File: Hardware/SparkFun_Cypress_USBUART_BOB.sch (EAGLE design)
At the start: 29 parts, among them J1 MICROB, J3 FTDI_BASICPTH, U1 CY7C65213, U2 MIC5219 3.3V

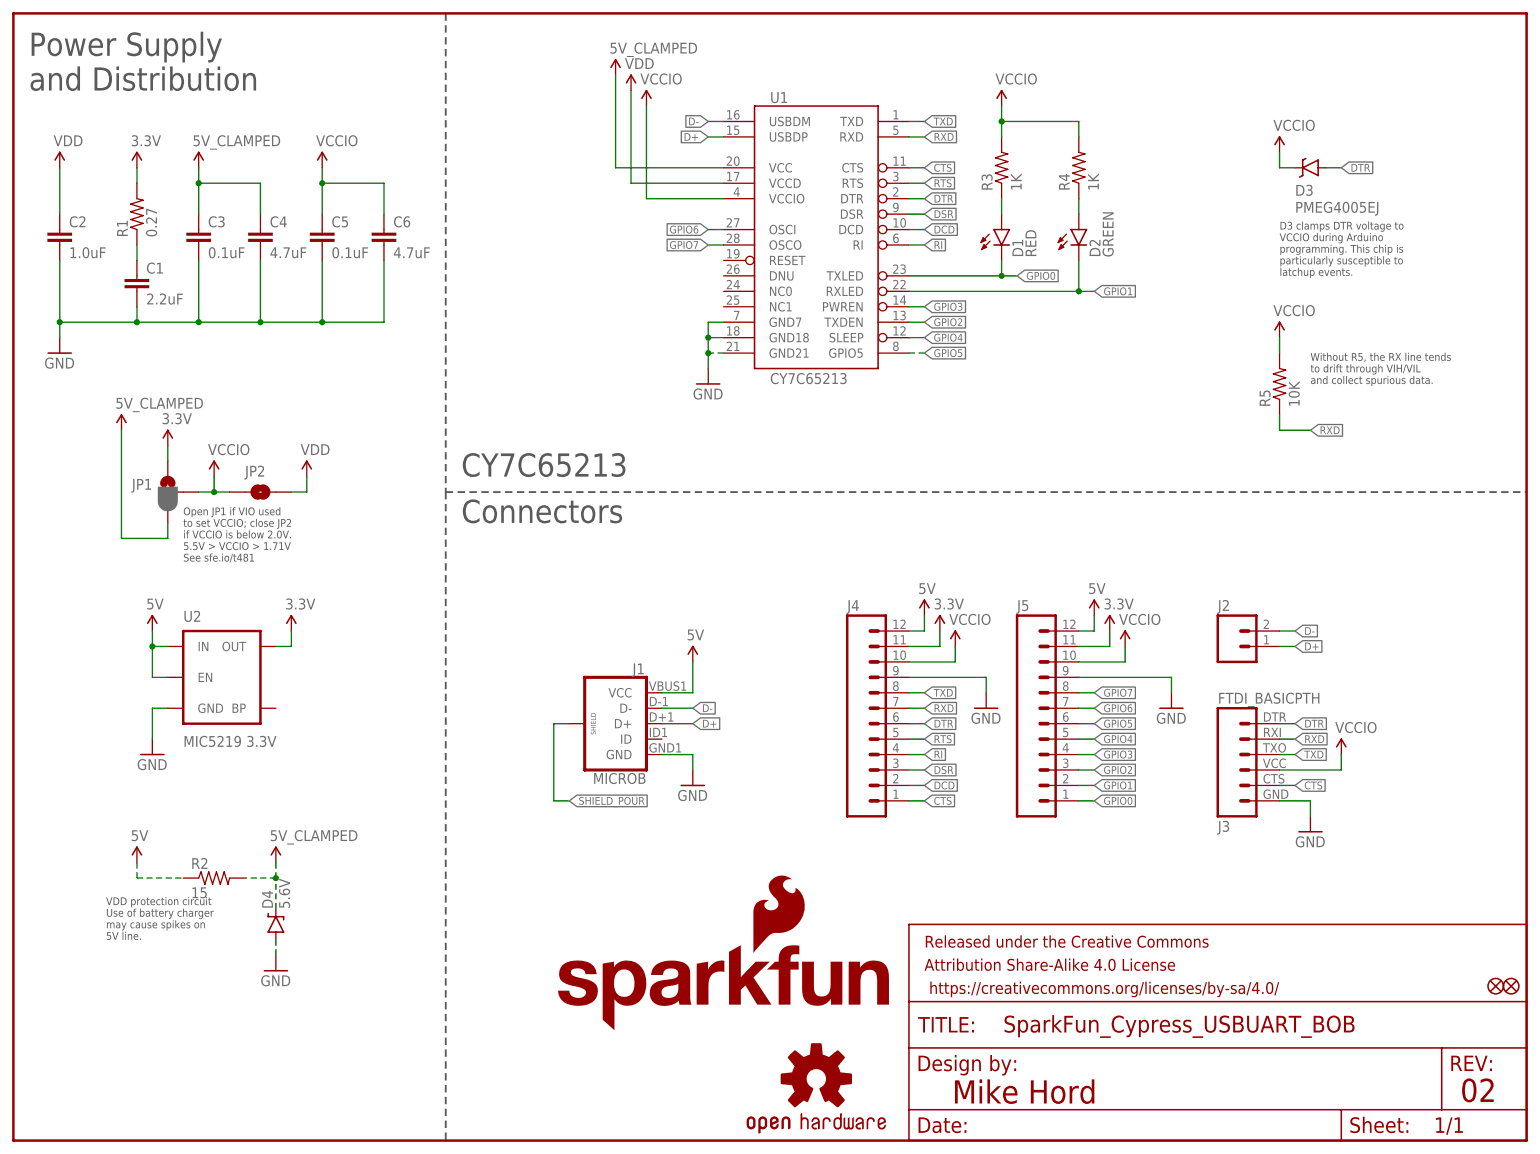
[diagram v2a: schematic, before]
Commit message: Feedback from group review, add clamping diodes
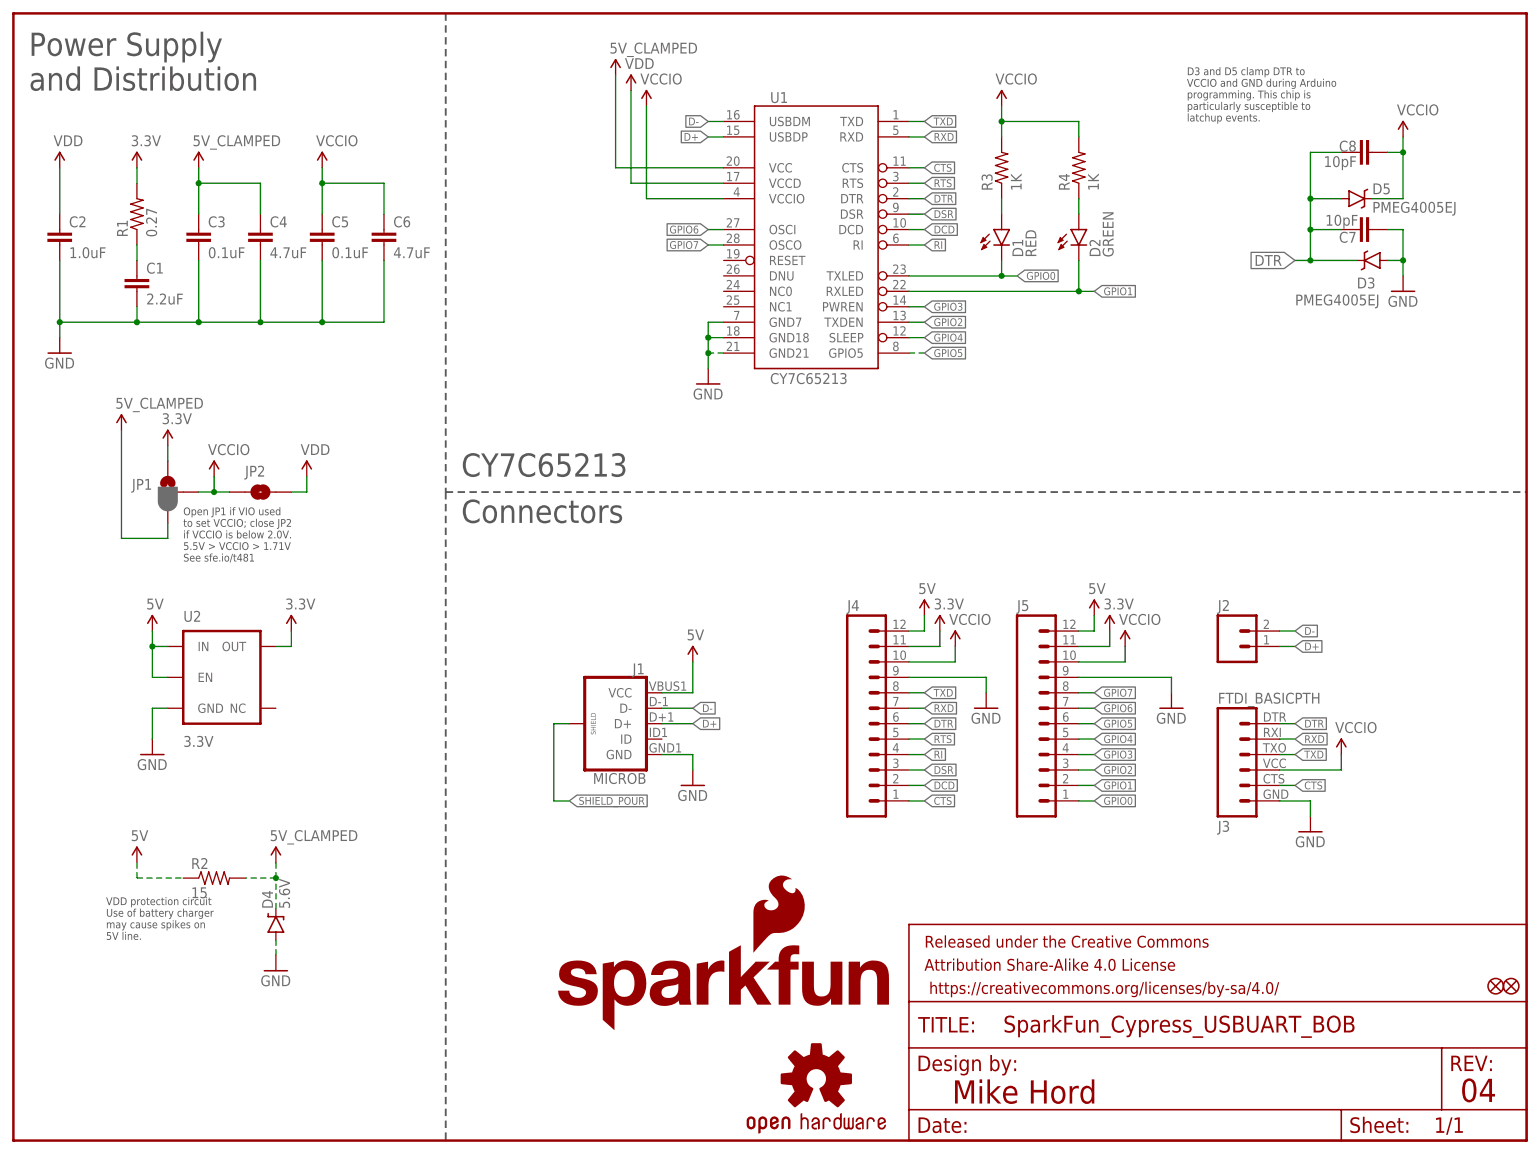
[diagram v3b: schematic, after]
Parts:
- removed R5: 10K, SparkFun-Resistors:10KOHM-1/10W-1%(0603)0603
- added C7, C8: 10pF, SparkFun-Capacitors:10PF-50V-5%(0603)
- added D5: PMEG4005EJ, SparkFun-DiscreteSemi:DIODE-SCHOTTKY-PMEG4005EJ
- U2: value MIC5219 3.3V -> 3.3V; device SparkFun-PowerIC:V_REG_MIC52193.3V -> SparkFun-PowerIC:V_REG_AP2112K-3.3V
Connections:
- net DTR: now also C7.1, C8.1, D3.C, D5.A; no longer D3.A
- net GND: now also C7.2, D3.A
- net RXD: no longer R5.1
- net VCCIO: now also C8.2, D5.C; no longer D3.C, R5.2
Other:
- note added: "04"
- note added: "D3 and D5 clamp DTR to VCCIO and GND during Arduino programming. This chip is particularly susceptible to latchup events."
- note removed: "02"
- note removed: "D3 clamps DTR voltage to VCCIO during Arduino programming. This chip is particularly susceptible to latchup events."
- note removed: "Without R5, the RX line tends to drift through VIH/VIL and collect spurious data."
- moved on the sheet: D3
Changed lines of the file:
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@@
 <layer number="255" name="routoute" color="7" fill="1" visible="yes" active="yes"/>
 </layers>
-<schematic xreflabel="%F%N/%S" xrefpart="1_/%S.%C%R">
+<schematic xreflabel="%F%N/%S" xrefpart="/%S.%C%R">
 <attributes>
 </attributes>
@@
 <part name="R1" library="SparkFun-Resistors" deviceset="0.27OHM-1/10W-1%(0603)" device="" value="0.27"/>
 <part name="C1" library="SparkFun-Capacitors" deviceset="2.2UF-10V-20%(0603)" device="" value="2.2uF"/>
-<part name="U2" library="SparkFun-PowerIC" deviceset="V_REG_MIC5219" device="3.3V" value="MIC5219 3.3V"/>
+<part name="U2" library="SparkFun-PowerIC" deviceset="V_REG_AP2112" device="K-3.3V" value="3.3V"/>
 <part name="J1" library="SparkFun-Connectors" deviceset="USB_MICROB_PLUG" device="CONN-11752" value="MICROB"/>
 <part name="J2" library="SparkFun-Connectors" deviceset="M02" device="PTH"/>
@@
 <part name="GND6" library="SparkFun-Aesthetics" deviceset="GND" device=""/>
 <part name="D3" library="SparkFun-DiscreteSemi" deviceset="DIODE-SCHOTTKY" device="-PMEG4005EJ" value="PMEG4005EJ"/>
-<part name="SUPPLY21" library="SparkFun-Aesthetics" deviceset="VCCIO" device=""/>
 <part name="GND7" library="SparkFun-Aesthetics" deviceset="GND" device=""/>
 <part name="SUPPLY22" library="SparkFun-Aesthetics" deviceset="VCCIO" device=""/>
@@
 <part name="SUPPLY23" library="SparkFun-Aesthetics" deviceset="VCCIO" device=""/>
 <part name="LOGO2" library="SparkFun-Aesthetics" deviceset="OSHW-LOGO" device="S"/>
-<part name="R5" library="SparkFun-Resistors" deviceset="10KOHM-1/10W-1%(0603)" device="0603" value="10K"/>
-<part name="SUPPLY24" library="SparkFun-Aesthetics" deviceset="VCCIO" device=""/>
+<part name="GND9" library="SparkFun-Aesthetics" deviceset="GND" device=""/>
+<part name="C7" library="SparkFun-Capacitors" deviceset="10PF-50V-5%(0603)" device="" value="10pF"/>
+<part name="D5" library="SparkFun-DiscreteSemi" deviceset="DIODE-SCHOTTKY" device="-PMEG4005EJ" value="PMEG4005EJ"/>
+<part name="C8" library="SparkFun-Capacitors" deviceset="10PF-50V-5%(0603)" device="" value="10pF"/>
+<part name="SUPPLY21" library="SparkFun-Aesthetics" deviceset="VCCIO" device=""/>
 </parts>
 <sheets>
 <sheet>
 <plain>
-<text x="237.998" y="6.35" size="3.81" layer="94" font="vector">02</text>
+<text x="237.998" y="6.35" size="3.81" layer="94" font="vector">04</text>
 <text x="154.432" y="6.096" size="3.81" layer="94" font="vector">Mike Hord</text>
 <text x="27.94" y="95.25" size="1.27" layer="97" font="vector">Open JP1 if VIO used
@@
 <text x="73.66" y="101.6" size="3.81" layer="97" font="vector">Connectors</text>
 <text x="73.66" y="109.22" size="3.81" layer="97" font="vector">CY7C65213</text>
-<text x="208.28" y="142.24" size="1.27" layer="97" font="vector">D3 clamps DTR voltage to
-VCCIO during Arduino
+<text x="193.04" y="167.64" size="1.27" layer="97" font="vector">D3 and D5 clamp DTR to
+VCCIO and GND during Arduino
 programming. This chip is
 particularly susceptible to
@@
 may cause spikes on
 5V line.</text>
-<text x="213.36" y="124.46" size="1.27" layer="97" font="vector">Without R5, the RX line tends
-to drift through VIH/VIL
-and collect spurious data.</text>
 </plain>
 <instances>
@@
 <instance part="J5" gate="G$1" x="165.1" y="71.12"/>
 <instance part="GND6" gate="1" x="190.5" y="71.12"/>
-<instance part="D3" gate="G$1" x="213.36" y="160.02" smashed="yes" rot="R180">
-<attribute name="NAME" x="210.82" y="155.4226" size="1.778" layer="95"/>
-<attribute name="VALUE" x="210.82" y="152.6286" size="1.778" layer="96"/>
+<instance part="D3" gate="G$1" x="223.52" y="144.78" smashed="yes" rot="R180">
+<attribute name="NAME" x="220.98" y="140.1826" size="1.778" layer="95"/>
+<attribute name="VALUE" x="210.82" y="137.3886" size="1.778" layer="96"/>
 </instance>
-<instance part="SUPPLY21" gate="G$1" x="208.28" y="162.56"/>
 <instance part="GND7" gate="1" x="213.36" y="50.8"/>
 <instance part="SUPPLY22" gate="G$1" x="218.44" y="63.5"/>
@@
 <instance part="SUPPLY23" gate="G$1" x="50.8" y="160.02"/>
 <instance part="LOGO2" gate="G$1" x="132.08" y="10.16"/>
-<instance part="R5" gate="G$1" x="208.28" y="124.46" rot="R90"/>
-<instance part="SUPPLY24" gate="G$1" x="208.28" y="132.08"/>
+<instance part="GND9" gate="1" x="228.6" y="139.7"/>
+<instance part="C7" gate="G$1" x="223.52" y="149.86" smashed="yes" rot="R90">
+<attribute name="NAME" x="220.98" y="149.479" size="1.778" layer="95" rot="R180"/>
+<attribute name="VALUE" x="221.234" y="152.273" size="1.778" layer="96" rot="R180"/>
+</instance>
+<instance part="D5" gate="G$1" x="220.98" y="154.94" smashed="yes">
+<attribute name="NAME" x="223.52" y="155.6766" size="1.778" layer="95"/>
+<attribute name="VALUE" x="223.52" y="152.6286" size="1.778" layer="96"/>
+</instance>
+<instance part="C8" gate="G$1" x="223.52" y="162.56" smashed="yes" rot="R90">
+<attribute name="NAME" x="220.98" y="164.465" size="1.778" layer="95" rot="R180"/>
+<attribute name="VALUE" x="220.98" y="161.925" size="1.778" layer="96" rot="R180"/>
+</instance>
+<instance part="SUPPLY21" gate="G$1" x="228.6" y="165.1"/>
 </instances>
 <busses>
@@
 <wire x1="43.18" y1="30.48" x2="43.18" y2="33.02" width="0.1524" layer="91" style="longdash"/>
 </segment>
+<segment>
+<pinref part="D3" gate="G$1" pin="A"/>
+<pinref part="GND9" gate="1" pin="GND"/>
+<wire x1="226.06" y1="144.78" x2="228.6" y2="144.78" width="0.1524" layer="91"/>
+<wire x1="228.6" y1="144.78" x2="228.6" y2="142.24" width="0.1524" layer="91"/>
+<pinref part="C7" gate="G$1" pin="2"/>
+<wire x1="226.06" y1="149.86" x2="228.6" y2="149.86" width="0.1524" layer="91"/>
+<wire x1="228.6" y1="149.86" x2="228.6" y2="144.78" width="0.1524" layer="91"/>
+<junction x="228.6" y="144.78"/>
+</segment>
 </net>
 <net name="5V" class="0">
@@
 </segment>
 <segment>
-<pinref part="SUPPLY21" gate="G$1" pin="VCCIO"/>
-<wire x1="208.28" y1="162.56" x2="208.28" y2="160.02" width="0.1524" layer="91"/>
-<pinref part="D3" gate="G$1" pin="C"/>
-<wire x1="208.28" y1="160.02" x2="210.82" y2="160.02" width="0.1524" layer="91"/>
-</segment>
-<segment>
 <pinref part="J3" gate="G$1" pin="4"/>
 <pinref part="SUPPLY22" gate="G$1" pin="VCCIO"/>
@@
 </segment>
 <segment>
-<pinref part="SUPPLY24" gate="G$1" pin="VCCIO"/>
-<pinref part="R5" gate="G$1" pin="2"/>
-<wire x1="208.28" y1="132.08" x2="208.28" y2="129.54" width="0.1524" layer="91"/>
+<pinref part="D5" gate="G$1" pin="C"/>
+<wire x1="228.6" y1="154.94" x2="223.52" y2="154.94" width="0.1524" layer="91"/>
+<pinref part="C8" gate="G$1" pin="2"/>
+<wire x1="226.06" y1="162.56" x2="228.6" y2="162.56" width="0.1524" layer="91"/>
+<wire x1="228.6" y1="162.56" x2="228.6" y2="154.94" width="0.1524" layer="91"/>
+<pinref part="SUPPLY21" gate="G$1" pin="VCCIO"/>
+<wire x1="228.6" y1="165.1" x2="228.6" y2="162.56" width="0.1524" layer="91"/>
+<junction x="228.6" y="162.56"/>
 </segment>
 </net>
@@
 </segment>
 <segment>
-<pinref part="D3" gate="G$1" pin="A"/>
-<wire x1="215.9" y1="160.02" x2="218.44" y2="160.02" width="0.1524" layer="91"/>
-<label x="218.44" y="160.02" size="1.27" layer="95" font="vector" xref="yes"/>
-</segment>
-<segment>
 <pinref part="J4" gate="G$1" pin="6"/>
 <wire x1="147.32" y1="68.58" x2="149.86" y2="68.58" width="0.1524" layer="91"/>
 <label x="149.86" y="68.58" size="1.27" layer="95" font="vector" xref="yes"/>
 </segment>
+<segment>
+<pinref part="D3" gate="G$1" pin="C"/>
+<wire x1="210.82" y1="144.78" x2="213.36" y2="144.78" width="0.1524" layer="91"/>
+<label x="210.82" y="144.78" size="1.778" layer="95" rot="R180" xref="yes"/>
+<pinref part="C7" gate="G$1" pin="1"/>
+<wire x1="213.36" y1="144.78" x2="220.98" y2="144.78" width="0.1524" layer="91"/>
+<wire x1="218.44" y1="149.86" x2="213.36" y2="149.86" width="0.1524" layer="91"/>
+<wire x1="213.36" y1="149.86" x2="213.36" y2="144.78" width="0.1524" layer="91"/>
+<junction x="213.36" y="144.78"/>
+<wire x1="213.36" y1="149.86" x2="213.36" y2="154.94" width="0.1524" layer="91"/>
+<junction x="213.36" y="149.86"/>
+<pinref part="D5" gate="G$1" pin="A"/>
+<wire x1="213.36" y1="154.94" x2="218.44" y2="154.94" width="0.1524" layer="91"/>
+<pinref part="C8" gate="G$1" pin="1"/>
+<wire x1="218.44" y1="162.56" x2="213.36" y2="162.56" width="0.1524" layer="91"/>
+<wire x1="213.36" y1="162.56" x2="213.36" y2="154.94" width="0.1524" layer="91"/>
+<junction x="213.36" y="154.94"/>
+</segment>
 </net>
 <net name="RTS" class="0">
@@
 <label x="210.82" y="66.04" size="1.27" layer="95" font="vector" rot="MR180" xref="yes"/>
 </segment>
-<segment>
-<pinref part="R5" gate="G$1" pin="1"/>
-<wire x1="208.28" y1="119.38" x2="208.28" y2="116.84" width="0.1524" layer="91"/>
-<wire x1="208.28" y1="116.84" x2="213.36" y2="116.84" width="0.1524" layer="91"/>
-<label x="213.36" y="116.84" size="1.27" layer="95" xref="yes"/>
-</segment>
-</net>
+</net>
